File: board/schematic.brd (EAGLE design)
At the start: 97.8 x 65.8 mm, 41 parts, among them IC1 STM32F207ZGT, IC3 LM3940, J1 DCJ0202, J3 DM3AT-SF-PEJM5

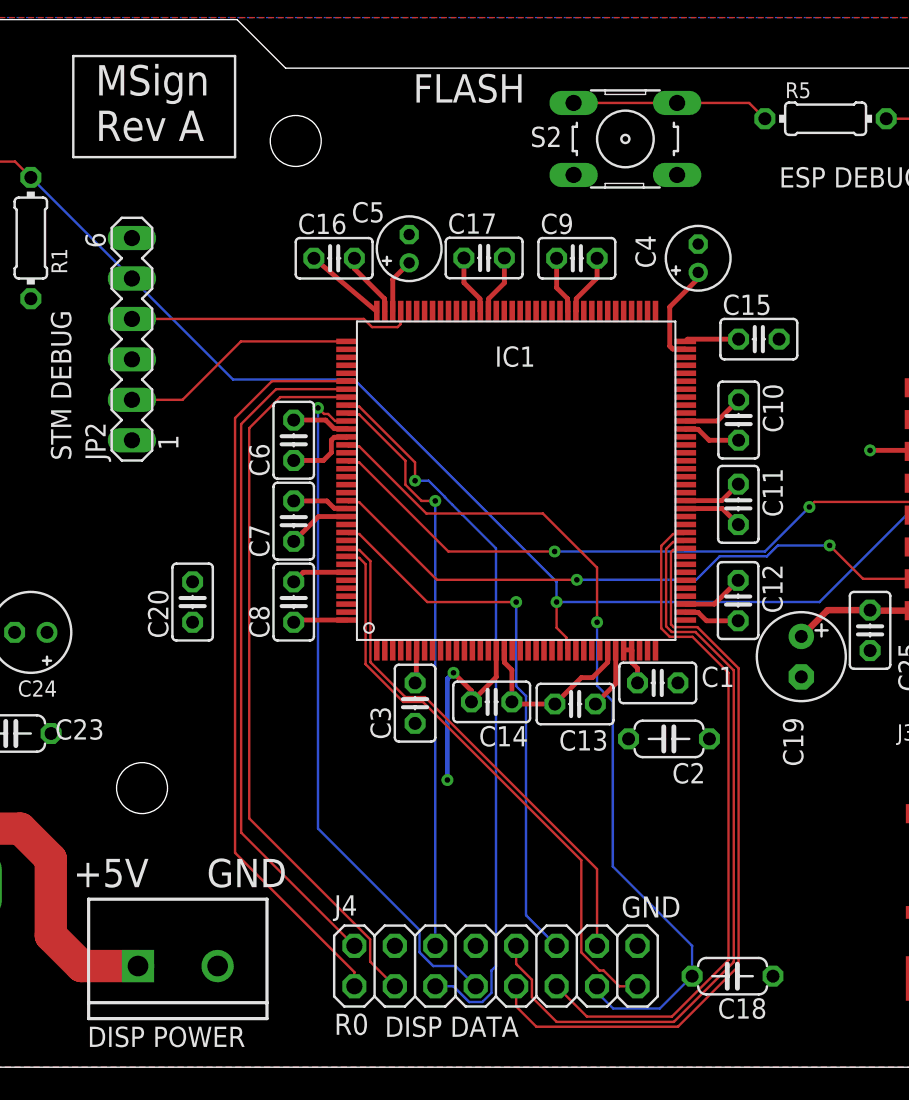
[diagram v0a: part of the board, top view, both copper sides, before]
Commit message: Update board to REV B
Fixes noise issues -- workaround: use a 470k resistor on C18 instead of
the cap.
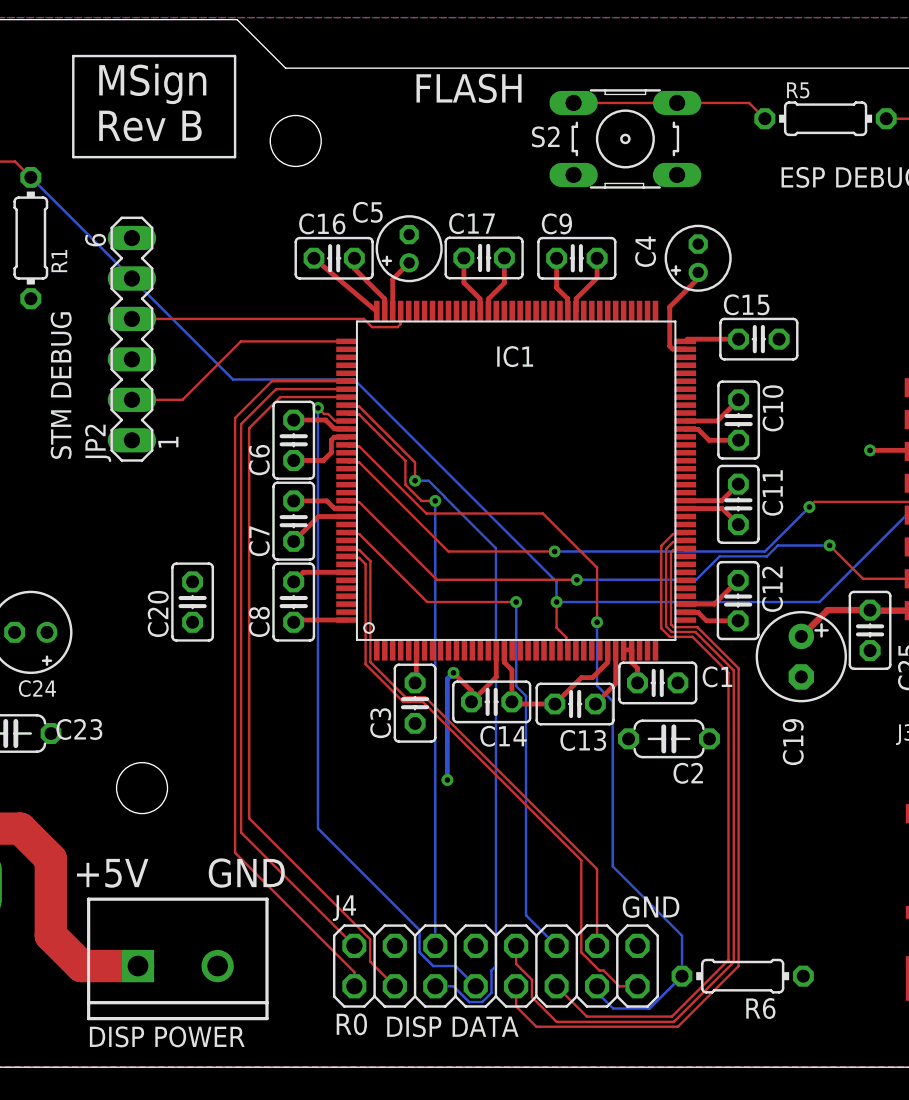
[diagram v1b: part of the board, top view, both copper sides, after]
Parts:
- removed C18: 10pF, rcl:C050-024X044
- added R6: 470K, rcl:0204/7
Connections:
- net DCLK: now also R6.2; no longer C18.2
- net GND: now also R6.1; no longer C18.1
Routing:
- net DCLK: track 54.6 -> 53.7 mm
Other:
- board text added: "MSign Rev B"
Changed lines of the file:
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@@
 <setting verticaltext="up"/>
 </settings>
-<grid distance="5" unitdist="mil" unit="mil" style="lines" multiple="1" display="no" altdistance="5" altunitdist="mil" altunit="mil"/>
+<grid distance="25" unitdist="mil" unit="mil" style="lines" multiple="1" display="no" altdistance="5" altunitdist="mil" altunit="mil"/>
 <layers>
 <layer number="1" name="Top" color="4" fill="1" visible="yes" active="yes"/>
@@
 <text x="76.2" y="7.62" size="1.778" layer="21">SD</text>
 <text x="19.304" y="58.166" size="1.905" layer="21">MSign
-Rev A</text>
+Rev B</text>
 <hole x="31.877" y="58.166" drill="3.2"/>
 <hole x="22.225" y="17.526" drill="3.2"/>
@@
 <attribute name="NAME" x="70.225" y="20.512" size="1.016" layer="25" ratio="12" align="bottom-center"/>
 </element>
-<element name="C18" library="rcl" library_urn="urn:adsk.eagle:library:334" package="C050-024X044" package3d_urn="urn:adsk.eagle:package:23643/1" value="10pF" x="59.309" y="5.715" smashed="yes" rot="R180">
-<attribute name="NAME" x="61.468" y="4.318" size="1.27" layer="25" ratio="10" rot="R180"/>
-<attribute name="SPICEPREFIX" value="C" x="59.309" y="5.715" size="1.778" layer="27" rot="R180" display="off"/>
-<attribute name="VALUE" x="61.468" y="8.382" size="1.27" layer="27" ratio="10" rot="R180"/>
+<element name="R6" library="rcl" library_urn="urn:adsk.eagle:library:334" package="0204/7" package3d_urn="urn:adsk.eagle:package:23498/1" value="470K" x="59.944" y="5.715" smashed="yes" rot="R180">
+<attribute name="NAME" x="62.103" y="4.318" size="1.27" layer="25" ratio="10" rot="R180"/>
+<attribute name="SPICEPREFIX" value="R" x="59.944" y="5.715" size="1.778" layer="27" rot="R180" display="off"/>
+<attribute name="VALUE" x="62.103" y="8.382" size="1.27" layer="27" ratio="10" rot="R180"/>
 </element>
 <element name="J2" library="SparkFun-Connectors" package="SCREWTERMINAL-5MM-2" value="" x="21.971" y="6.35" smashed="yes">
@@
 <wire x1="35.8646875" y1="38.9836" x2="40.0784875" y2="34.7698" width="0.1524" layer="1"/>
 <wire x1="51.7906" y1="22.9657875" x2="51.7906" y2="12.5984" width="0.1524" layer="16"/>
-<wire x1="51.7906" y1="12.5984" x2="56.769" y2="7.62" width="0.1524" layer="16"/>
 <wire x1="47.3992" y1="34.7698" x2="50.8" y2="31.369" width="0.1524" layer="1"/>
 <wire x1="50.8" y1="31.369" x2="50.8" y2="27.94" width="0.1524" layer="1"/>
 <wire x1="40.0784875" y1="34.7698" x2="47.3992" y2="34.7698" width="0.1524" layer="1"/>
 <contactref element="J4" pad="13"/>
-<contactref element="C18" pad="2"/>
-<wire x1="56.769" y1="7.62" x2="56.769" y2="5.715" width="0.1524" layer="16"/>
-<wire x1="56.769" y1="5.715" x2="54.737" y2="3.683" width="0.1524" layer="16"/>
-<wire x1="54.737" y1="3.683" x2="51.816" y2="3.683" width="0.1524" layer="16"/>
+<contactref element="R6" pad="2"/>
+<wire x1="53.975" y1="3.683" x2="51.816" y2="3.683" width="0.1524" layer="16"/>
 <wire x1="51.816" y1="3.683" x2="50.8" y2="4.699" width="0.1524" layer="16"/>
 <wire x1="50.8" y1="4.699" x2="50.8" y2="5.08" width="0.1524" layer="16"/>
+<wire x1="51.7906" y1="12.5984" x2="56.134" y2="8.255" width="0.1524" layer="16"/>
+<wire x1="56.134" y1="8.255" x2="56.134" y2="5.715" width="0.1524" layer="16"/>
+<wire x1="56.134" y1="5.715" x2="54.102" y2="3.683" width="0.1524" layer="16"/>
+<wire x1="54.102" y1="3.683" x2="53.975" y2="3.683" width="0.1524" layer="16"/>
 </signal>
 <signal name="A">
@@
 <contactref element="J3" pad="6"/>
 <contactref element="J3" pad="MOUNT2"/>
-<contactref element="C18" pad="1"/>
+<contactref element="R6" pad="1"/>
 <contactref element="J2" pad="2"/>
 <contactref element="C25" pad="2"/>

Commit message: bord redisgn
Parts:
- removed C10, C11, C12, C13, C14, C15, C16, C17, C8, C9: 100nF, rcl:C025-025X050
- removed IC1: STM32F207ZGT, micro-stm_v3:LQFP144
- added IC4: STM32F205RGT, micro-stm_v3:LQFP64
- moved C4 104.7 mm to (-13.3, -26.7), turned to 0 degrees
- moved C2 98.6 mm to (-12.1, -51.4), turned to 0 degrees
- moved C5 98.2 mm to (-13.3, -31.8), turned to 0 degrees
- moved C3 96.5 mm to (-12.7, -58.4), turned to 0 degrees
- moved C1 91.2 mm to (-12.7, -37.5), turned to 0 degrees
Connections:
- new net N$4: C1.2, C2.2, C3.2, IC4.1, IC4.13
- net +3V3: now also IC4.19, IC4.32, IC4.48, IC4.64; no longer C1.2, C10.1, C11.1, C12.1, C13.1, C14.1, C15.1, C16.1, C17.1, C2.2, C3.2, C8.1, C9.1, IC1.108, IC1.121, IC1.131, IC1.144, IC1.17, IC1.30, IC1.32, IC1.33, IC1.39, IC1.52, IC1.6, IC1.62, IC1.72, IC1.84, IC1.95
- net A: now also IC4.26; no longer IC1.46
- net B: now also IC4.27; no longer IC1.47
- net B0: now also IC4.10; no longer IC1.116
- net B1: now also IC4.25; no longer IC1.119
- net C: now also IC4.28; no longer IC1.48
- net D: now also IC4.55; no longer IC1.133
- net DCLK: now also IC4.37; no longer IC1.122
- net G0: now also IC4.9; no longer IC1.115
- net G1: now also IC4.24; no longer IC1.118
- net GND: now also IC4.12, IC4.18, IC4.60, IC4.63; no longer C10.2, C11.2, C12.2, C13.2, C14.2, C15.2, C16.2, C17.2, C8.2, C9.2, IC1.107, IC1.120, IC1.130, IC1.138, IC1.16, IC1.31, IC1.38, IC1.51, IC1.61, IC1.83, IC1.94
- net LAT: now also IC4.57; no longer IC1.135
- net N$2: now also IC4.31; no longer IC1.106
- net N$3: now also IC4.47; no longer IC1.71
- net OE: now also IC4.58; no longer IC1.136
- net R0: now also IC4.8; no longer IC1.114
- net R1: now also IC4.11; no longer IC1.117
- net RESET: now also IC4.7; no longer IC1.25
- net RX: now also IC4.17; no longer IC1.124
- net SWCLK: now also IC4.49; no longer IC1.109
- net SWDIO: now also IC4.46; no longer IC1.105
- net TX: now also IC4.16; no longer IC1.129
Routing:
- net RESET: track 105.8 -> 0.00 mm, vias 2 -> 0
- net +3V3: track 77.1 -> 0.00 mm, vias 1 -> 0
- net RX: track 74.5 -> 0.00 mm, vias 2 -> 0
- net FLASH: track 55.5 -> 0.00 mm
- net DCLK: track 53.7 -> 0.00 mm, vias 1 -> 0
- net GND: track 50.5 -> 0.00 mm, vias 2 -> 0
- net B: track 48.5 -> 0.00 mm
- net A: track 47.0 -> 0.00 mm
- net R0: track 46.8 -> 0.00 mm
- net R1: track 46.0 -> 0.00 mm, vias 1 -> 0
- net B0: track 45.8 -> 0.00 mm
- net C: track 43.5 -> 0.00 mm
- net B1: track 43.4 -> 0.00 mm, vias 1 -> 0
- net G0: track 43.3 -> 0.00 mm
- net TX: track 39.8 -> 0.00 mm, vias 2 -> 0
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
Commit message: c
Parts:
- removed J4: (no value), pinhead:2X08
- added IC1, IC5: 74HCT244DW, 74xx-eu:SO20W
- added J5: (no value), pinhead:2X08
- R6: value 470K -> 470k
- moved R6 114.9 mm to (-10.8, -84.8), turned to 0 degrees
- moved C5 107.9 mm to (58.4, 48.9)
- moved C2 99.1 mm to (40.3, 32.7)
- moved C4 98.5 mm to (43.2, 54.0), turned to 90 degrees
- moved C1 90.2 mm to (40.3, 35.6)
- moved IC4 83.2 mm to (46.4, 45.1)
- moved C7 25.7 mm to (55.9, 43.2), turned to 270 degrees
- moved C20 14.3 mm to (33.0, 41.3)
- moved C6 5.43 mm to (36.8, 41.3)
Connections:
- new net A_H: IC1.9, J5.9
- new net B0_H: IC1.16, J5.3
- new net B1_H: IC1.12, J5.7
- new net B_H: IC5.14, J5.10
- new net C_H: IC1.7, J5.11
- new net DCLK_H: IC1.5, J5.13, R6.2
- new net D_H: IC5.12, J5.12
- new net G0_H: IC5.18, J5.2
- new net G1_H: IC5.16, J5.6
- new net LAT_H: IC5.9, J5.14
- new net OE_H: IC1.3, J5.15
- new net R0_H: IC1.18, J5.1
- new net R1_H: IC1.14, J5.5
- net +5V: now also IC1.20, IC5.20
- net A: now also IC1.11; no longer J4.9
- net B: now also IC5.6; no longer J4.10
- net B0: now also IC1.4; no longer J4.3
- net B1: now also IC1.8; no longer J4.7
- net C: now also IC1.13; no longer J4.11
- net D: now also IC5.8; no longer J4.12
- net DCLK: now also IC1.15; no longer J4.13, R6.2
- net G0: now also IC5.2; no longer J4.2
- net G1: now also IC5.4; no longer J4.6
- net GND: now also IC1.1, IC1.10, IC1.19, IC5.1, IC5.10, IC5.19, J5.16, J5.4, J5.8; no longer J4.16, J4.4, J4.8
- net LAT: now also IC5.11; no longer J4.14
- net OE: now also IC1.17; no longer J4.15
- net R0: now also IC1.2; no longer J4.1
- net R1: now also IC1.6; no longer J4.5
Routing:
- net RX: track 0.00 -> 43.0 mm
- net R0: track 0.00 -> 32.2 mm
- net B0: track 0.00 -> 31.2 mm
- net R1: track 0.00 -> 30.6 mm
- net TX: track 0.00 -> 24.6 mm
- net GND: track 0.00 -> 20.2 mm
- net +3V3: track 0.00 -> 16.3 mm, vias 0 -> 2
- net N$4: track 0.00 -> 15.7 mm
- net N$1: track 0.00 -> 12.4 mm
- net FLASH: track 0.00 -> 7.80 mm
- net N$2: track 0.00 -> 5.66 mm
- net DEBUG_TX: track 0.00 -> 5.53 mm
- net G0: track 0.00 -> 4.78 mm, vias 0 -> 2
- net N$3: track 0.00 -> 2.28 mm

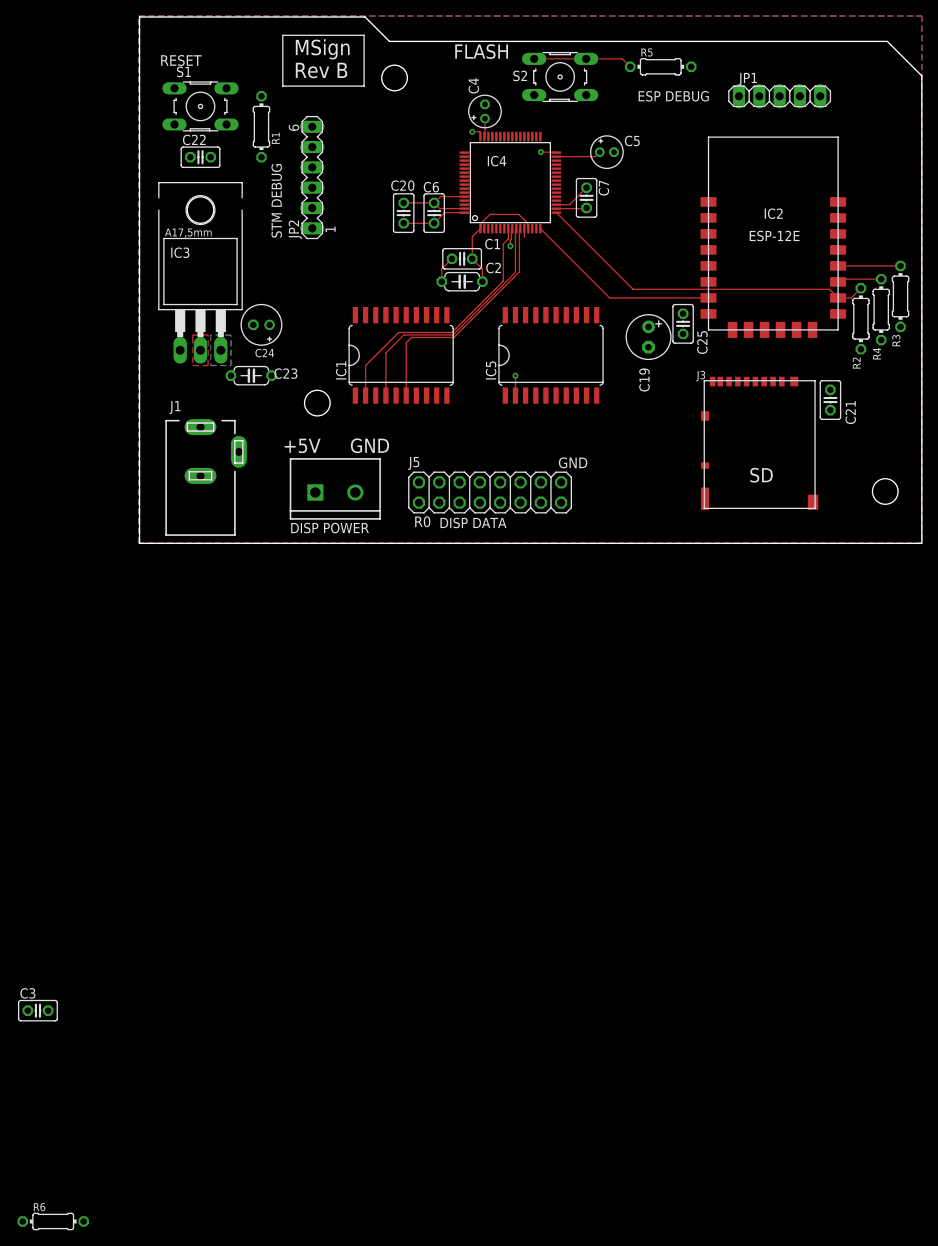
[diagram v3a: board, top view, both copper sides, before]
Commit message: board rev b minus button board connectors
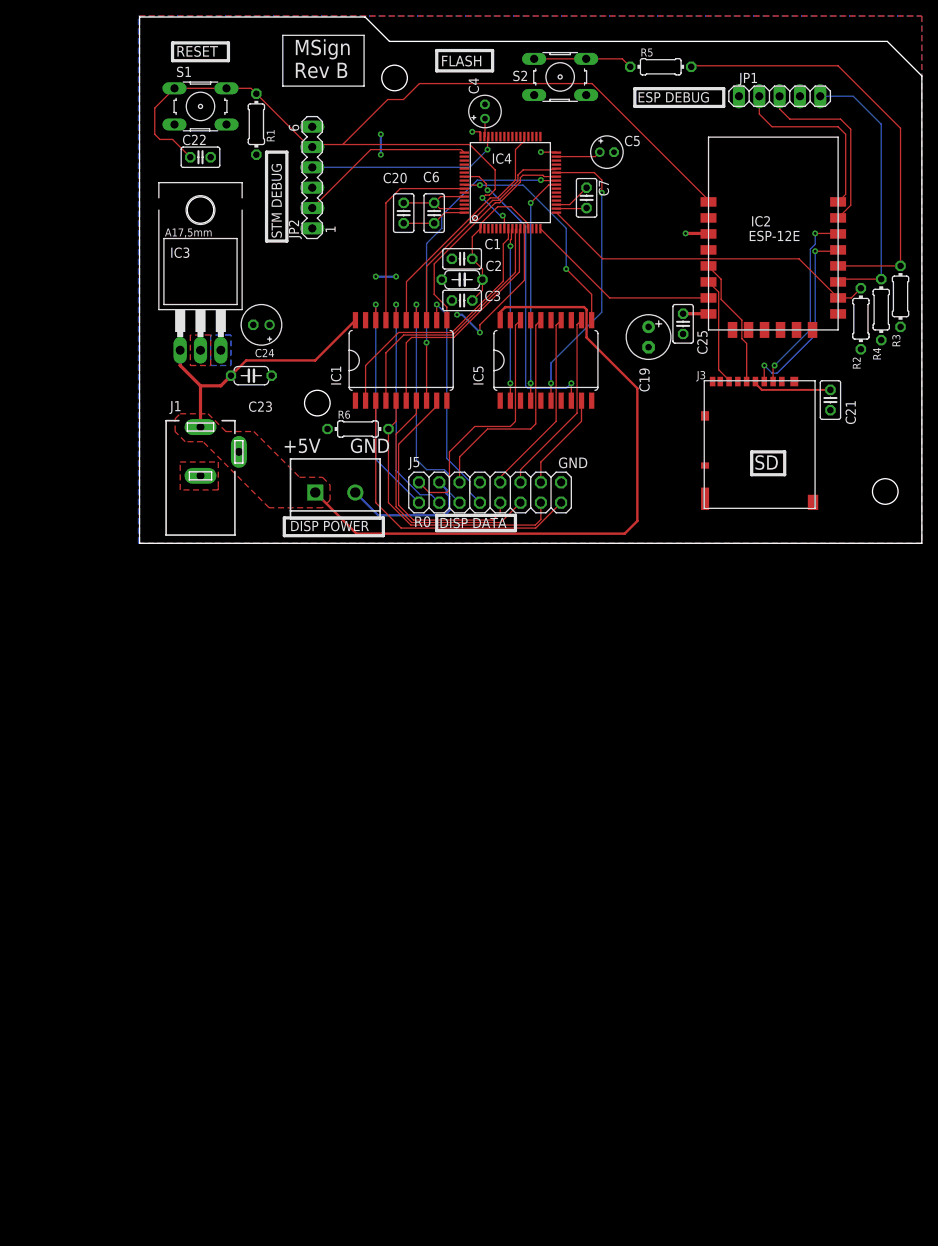
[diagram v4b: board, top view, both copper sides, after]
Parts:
- moved R6 106.1 mm to (27.3, 14.3)
- moved C3 103.4 mm to (40.3, 30.4)
- moved IC5 0.90 mm to (50.8, 22.9)
- moved R1 0.71 mm to (14.6, 52.4)
- moved IC1 0.64 mm to (32.7, 22.9)
- moved C2 0.25 mm to (40.3, 33.0)
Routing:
- net RESET: track 0.00 -> 121.7 mm, vias 0 -> 2
- net +5V: track 0.00 -> 117.7 mm
- net FLASH: track 7.80 -> 54.5 mm
- net B1: track 0.00 -> 40.1 mm, vias 0 -> 2
- net D: track 0.00 -> 38.8 mm, vias 0 -> 2
- net OE_H: track 0.00 -> 38.6 mm
- net GND: track 20.2 -> 57.2 mm, vias 0 -> 6
- net B: track 0.00 -> 36.3 mm, vias 0 -> 2
- net DCLK_H: track 0.00 -> 35.8 mm
- net G0_H: track 0.00 -> 32.0 mm
- net C_H: track 0.00 -> 31.7 mm
- net R1_H: track 0.00 -> 30.3 mm, vias 0 -> 1
- net A_H: track 0.00 -> 30.2 mm
- net B0_H: track 0.00 -> 29.8 mm, vias 0 -> 1
- net DCLK: track 0.00 -> 29.6 mm
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- added copper zone on layer 1, net +5V
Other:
- board text removed: "MSign Rev A"
